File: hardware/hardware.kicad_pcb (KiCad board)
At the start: 2 copper layers, 126.5 x 76.2 mm, 6 parts, among them U2 Teensy4.1_DEV-16771, U3 OKI-78SR-3.3_1.5-W36H-C, U4 LT1910, U5 LT1910, U6 LT1910

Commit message: Initial Rev2 Design
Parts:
- removed Bottom Text: MRDT, MRDT_Silkscreens:0_MRDT_Logo_20mm
- added D1: LED, LED_SMD:LED_0603_1608Metric_Pad1.05x0.95mm_HandSolder, F.Cu at (53.2, 83.3)
- added D2: LED, LED_SMD:LED_0603_1608Metric_Pad1.05x0.95mm_HandSolder, F.Cu at (71.3, 83.1)
- added D3: LED, LED_SMD:LED_0603_1608Metric_Pad1.05x0.95mm_HandSolder, F.Cu at (92.3, 78.5)
- added D4: LED, LED_SMD:LED_0603_1608Metric_Pad1.05x0.95mm_HandSolder, F.Cu at (117.7, 78.5)
- added D5: LED, LED_SMD:LED_0603_1608Metric_Pad1.05x0.95mm_HandSolder, F.Cu at (136.8, 78.5)
- added D6: LED, LED_SMD:LED_0603_1608Metric_Pad1.05x0.95mm_HandSolder, F.Cu at (92.3, 81.3)
- added D7: LED, LED_SMD:LED_0603_1608Metric_Pad1.05x0.95mm_HandSolder, F.Cu at (117.7, 80.3)
- added D8: LED, LED_SMD:LED_0603_1608Metric_Pad1.05x0.95mm_HandSolder, F.Cu at (136.9, 80.3)
- added D9: LED, LED_SMD:LED_0603_1608Metric_Pad1.05x0.95mm_HandSolder, F.Cu at (77.7, 59.2)
- added R10: 120, Resistor_SMD:R_0603_1608Metric_Pad0.98x0.95mm_HandSolder, F.Cu at (99.3, 78.5)
- added R11: 120, Resistor_SMD:R_0603_1608Metric_Pad0.98x0.95mm_HandSolder, F.Cu at (122.4, 78.5)
- added R12: 120, Resistor_SMD:R_0603_1608Metric_Pad0.98x0.95mm_HandSolder, F.Cu at (140.5, 78.5)
- added R4: 1000, Resistor_SMD:R_0603_1608Metric_Pad0.98x0.95mm_HandSolder, F.Cu at (77.7, 63.5)
- added R5: 300, Resistor_SMD:R_0603_1608Metric_Pad0.98x0.95mm_HandSolder, F.Cu at (58.2, 83.3)
- added R6: 120, Resistor_SMD:R_0603_1608Metric_Pad0.98x0.95mm_HandSolder, F.Cu at (75.0, 83.1)
- added R7: 120, Resistor_SMD:R_0603_1608Metric_Pad0.98x0.95mm_HandSolder, F.Cu at (99.3, 81.3)
- added R8: 120, Resistor_SMD:R_0603_1608Metric_Pad0.98x0.95mm_HandSolder, F.Cu at (114.0, 80.3)
- added R9: 120, Resistor_SMD:R_0603_1608Metric_Pad0.98x0.95mm_HandSolder, F.Cu at (133.2, 80.3)
- moved U6 46.2 mm to (138.8, 74.8)
- moved U5 23.7 mm to (117.2, 74.8)
- moved U4 5.91 mm to (92.7, 74.8)
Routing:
- net /Mosfets and Sensors/pair3_in: track 68.7 -> 38.6 mm, vias 1 -> 2
- net +5V: track 114.1 -> 142.9 mm, vias 6 -> 9
- net Net-(R8-Pad1): track 0.00 -> 24.2 mm, vias 0 -> 3
- net Net-(R7-Pad1): track 0.00 -> 23.1 mm, vias 0 -> 1
- net Net-(R9-Pad1): track 0.00 -> 22.3 mm, vias 0 -> 1
- net /Mosfets and Sensors/pair2_in: track 52.9 -> 38.3 mm, vias 1 -> 2
- net Net-(Conn7-Pad1): track 42.3 -> 27.8 mm
- net Net-(Conn4-Pad1): track 43.8 -> 30.9 mm
- net /Mosfets and Sensors/pair1_in: track 35.6 -> 46.7 mm, vias 1 -> 3
- net Net-(Conn10-Pad1): track 45.2 -> 34.4 mm, vias 3 -> 2
- net Net-(D6-Pad2): track 0.00 -> 5.18 mm
- net Net-(D3-Pad2): track 0.00 -> 5.18 mm
- net +3V3: track 231.6 -> 226.5 mm, vias 8 -> 5
- net Net-(D1-Pad2): track 0.00 -> 3.15 mm
- net Net-(D4-Pad2): track 0.00 -> 2.90 mm
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
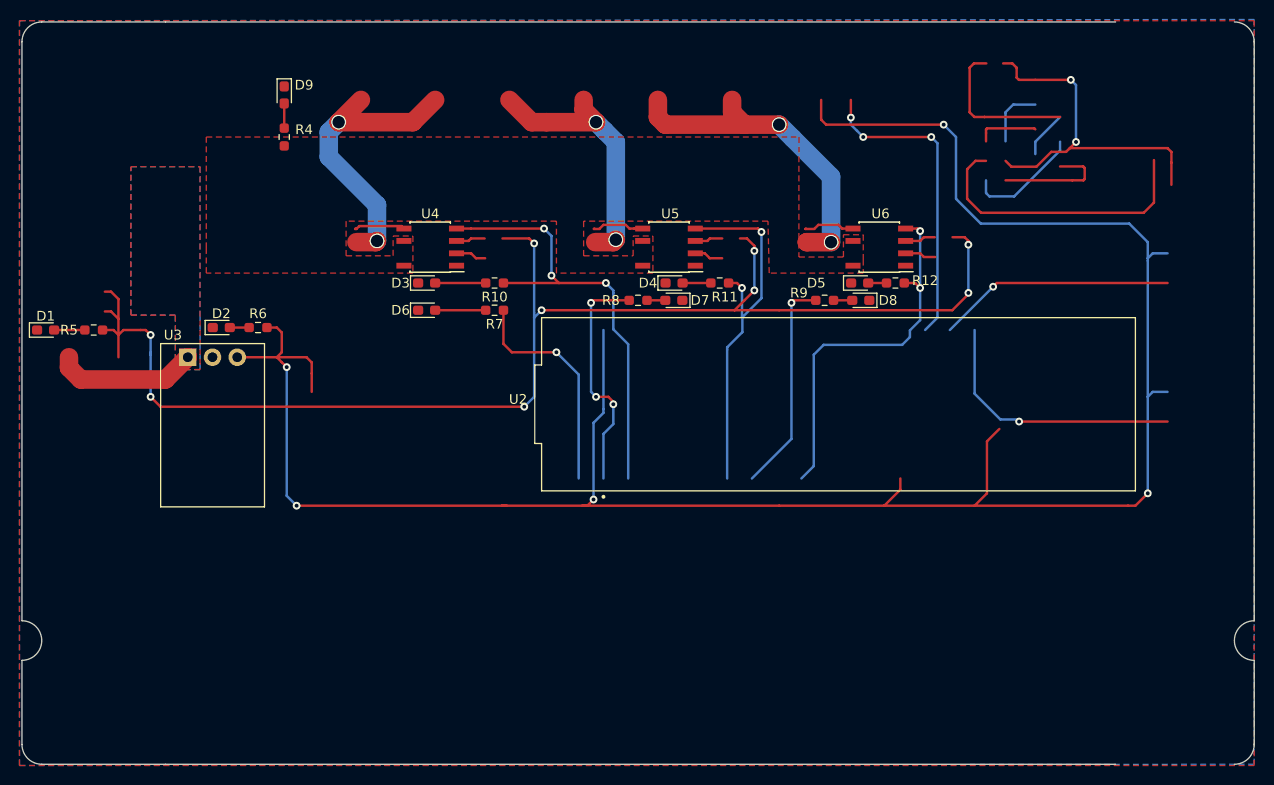
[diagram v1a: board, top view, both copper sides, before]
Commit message: Adjusted heating block connections
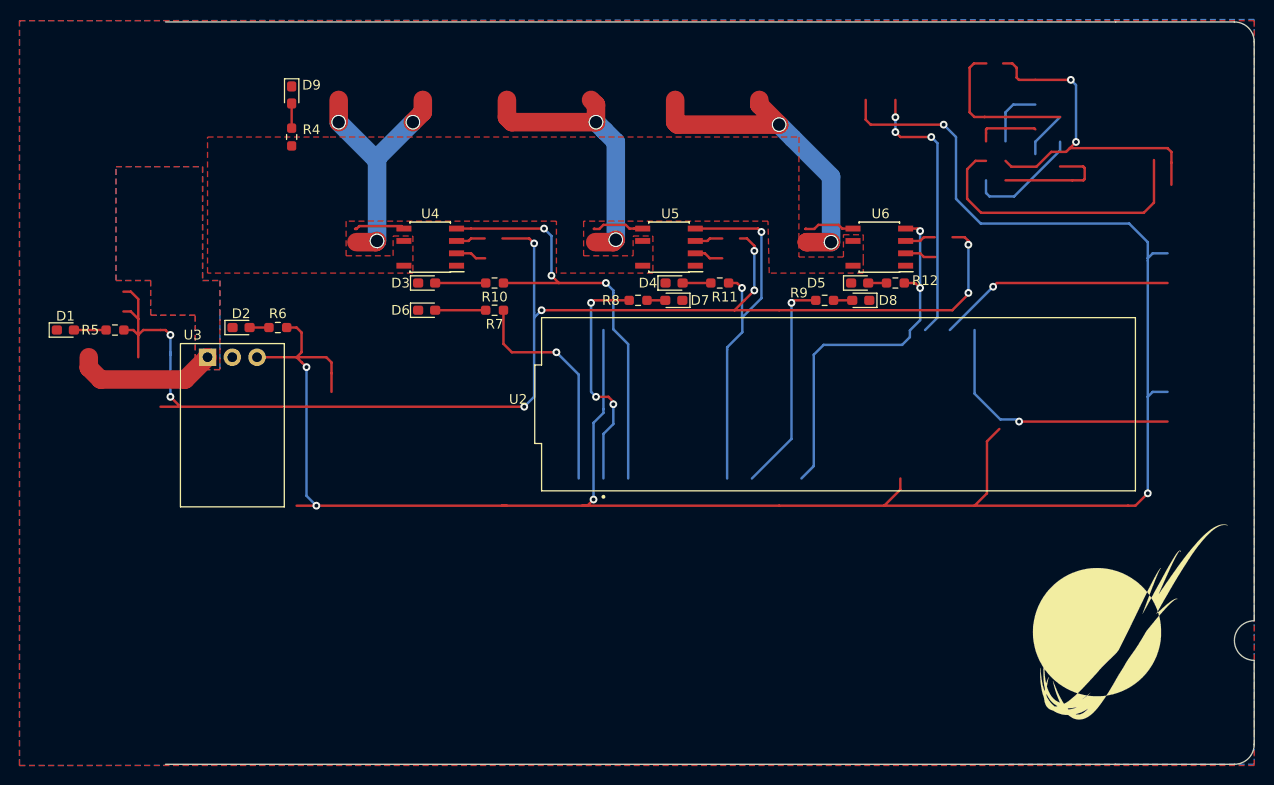
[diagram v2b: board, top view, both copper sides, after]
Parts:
- added G***: LOGO, MRDT_Silkscreens:0_MRDT_Logo_20mm, F.Cu at (164.6, 113.3)
- moved R5 2.18 mm to (60.3, 83.3)
- moved D2 2.03 mm to (73.3, 83.1)
- moved D1 2.03 mm to (55.3, 83.3)
- moved R6 2.03 mm to (77.1, 83.1)
- moved U3 2.03 mm to (69.8, 86.1)
- moved D9 0.76 mm to (78.5, 59.2)
- moved R4 0.76 mm to (78.5, 63.5)
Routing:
- net Net-(Conn4-Pad1): track 30.9 -> 26.3 mm, vias 2 -> 3
- net +3V3: track 226.5 -> 221.9 mm
- net /Mosfets and Sensors/pair1_out: track 31.9 -> 27.8 mm
- net Net-(Conn10-Pad1): track 34.4 -> 33.2 mm
- net Net-(Conn7-Pad1): track 27.8 -> 28.8 mm
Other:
- board size 126.5 x 76.2 mm -> 111.8 x 76.2 mm

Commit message: Fixed Mosfet LEDs
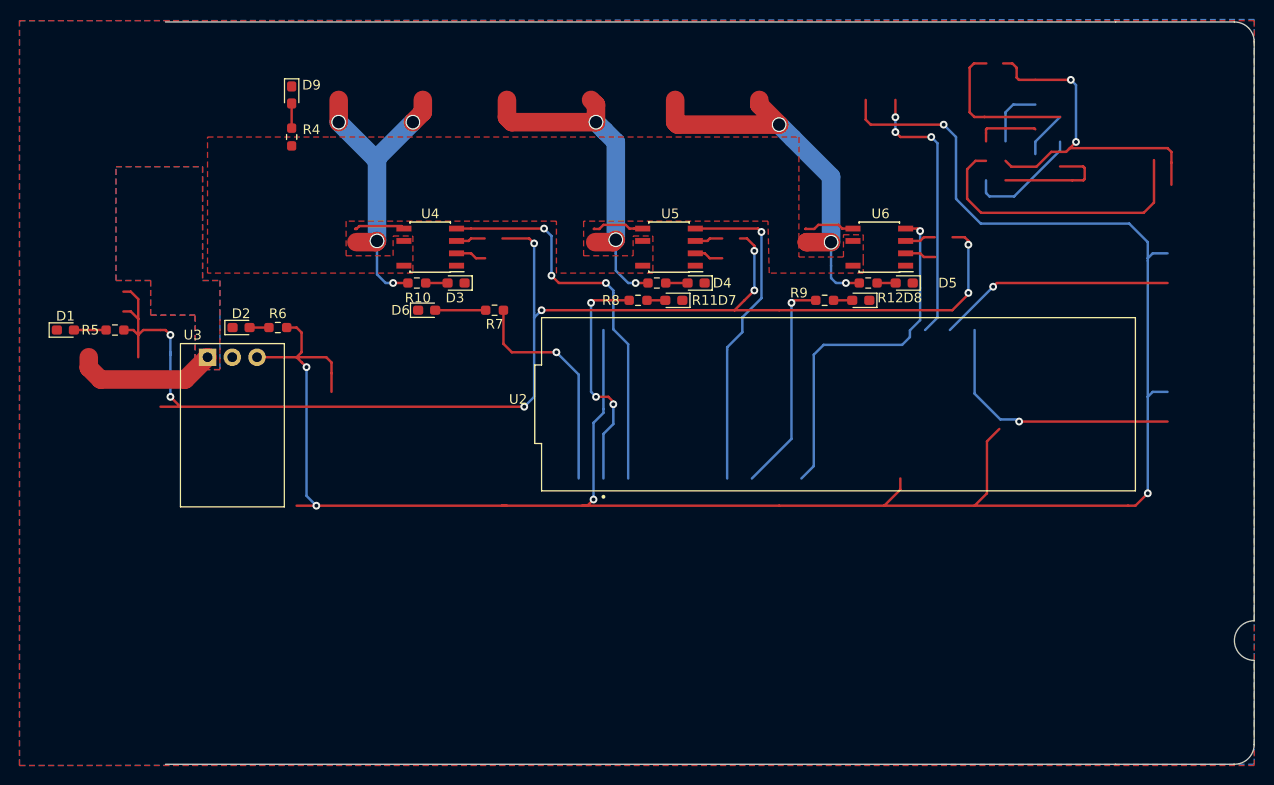
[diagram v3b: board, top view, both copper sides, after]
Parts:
- removed G***: LOGO, MRDT_Silkscreens:0_MRDT_Logo_20mm
- R10, R11, R12: value 120 -> 1000
- moved R10 7.98 mm to (91.3, 78.5), turned to 0 degrees
- moved R11 6.45 mm to (116.0, 78.5), turned to 0 degrees
- moved D5 4.57 mm to (141.4, 78.5), turned to 180 degrees
- moved D3 3.02 mm to (95.4, 78.5), turned to 180 degrees
- moved R12 2.79 mm to (137.7, 78.5), turned to 0 degrees
- moved D4 2.26 mm to (120.0, 78.5), turned to 180 degrees
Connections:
- R10 pad 1: /Mosfets and Sensors/pair1_in -> Net-(Conn4-Pad1)
- R11 pad 1: /Mosfets and Sensors/pair2_in -> Net-(Conn7-Pad1)
- R12 pad 1: /Mosfets and Sensors/pair3_in -> Net-(Conn10-Pad1)
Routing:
- net Net-(Conn7-Pad1): track 28.8 -> 35.8 mm, vias 2 -> 3
- net Net-(Conn4-Pad1): track 26.3 -> 33.3 mm, vias 3 -> 4
- net Net-(Conn10-Pad1): track 33.2 -> 40.0 mm, vias 2 -> 3
- net /Mosfets and Sensors/pair1_in: track 46.7 -> 41.0 mm
- net /Mosfets and Sensors/pair2_in: track 38.3 -> 33.7 mm, vias 2 -> 1
- net Net-(D3-Pad2): track 5.18 -> 2.24 mm
- net /Mosfets and Sensors/pair3_in: track 38.6 -> 36.8 mm, vias 2 -> 1
- net Net-(D4-Pad2): track 2.90 -> 2.24 mm
